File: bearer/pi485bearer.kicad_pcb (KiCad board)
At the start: 2 copper layers, 62 x 30 mm, 21 parts, among them P1 PWR, P2 Rasperry Pi, P3 Latch Disable, P4 TERM, P5 CONN_01X04, P6 CONN_01X04, Q1 2N4401, Q2 2N4401, Q3 2N4401, U1 NE555

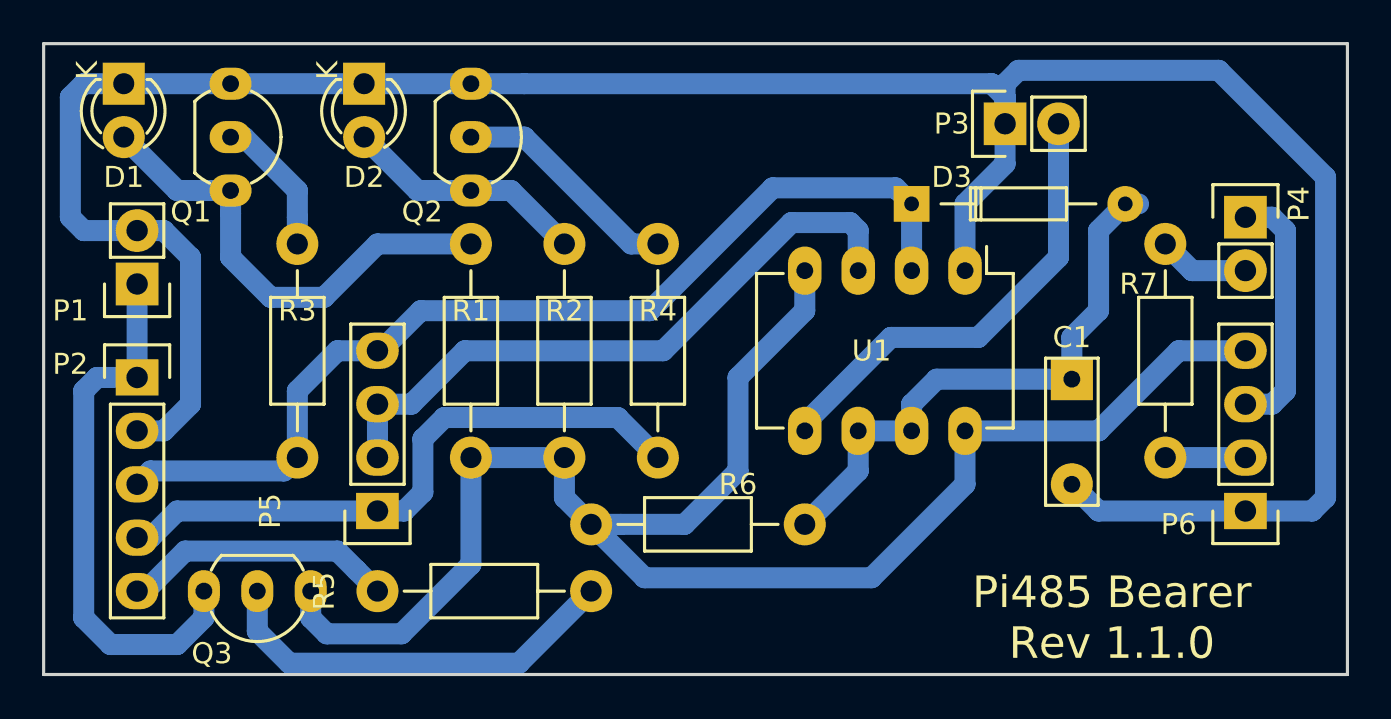
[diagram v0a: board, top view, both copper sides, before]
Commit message: Updated bearer with mount holes
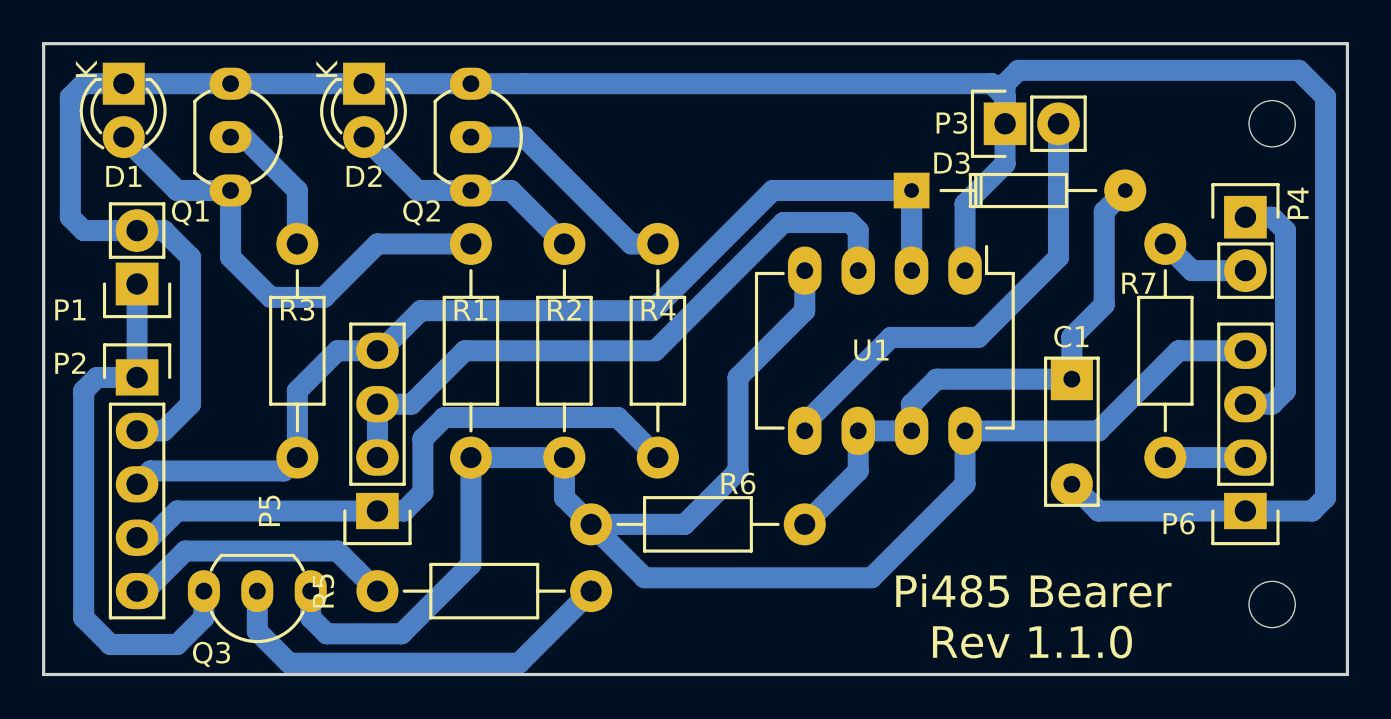
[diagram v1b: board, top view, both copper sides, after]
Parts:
- added MNT01: MountingHole_2.2mm_M2, Mounting_Holes:MountingHole_2.2mm_M2, F.Cu at (95.9, 24.8)
- added MNT02: MountingHole_2.2mm_M2, Mounting_Holes:MountingHole_2.2mm_M2, F.Cu at (95.9, 47.6)
- moved D3 0.63 mm to (78.7, 27.9)
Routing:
- net /(TXDO)_GPIO14: track 48.0 -> 51.7 mm
- net GND: track 123.9 -> 126.1 mm
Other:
- net class Default: trace_width 0.8 -> 1
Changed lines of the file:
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@@
 (kicad_pcb (version 20160815) (host pcbnew "(2016-12-18 revision 3ffa37c)-master")
   (general
-    (links 41)
+    (links 0)
     (no_connects 0)
     (area 37.389999 20.879999 99.540001 51.119002)
@@
     (tracks 142)
     (zones 0)
-    (modules 21)
+    (modules 23)
     (nets 18)
   )
@@
   )
   (setup
-    (last_trace_width 0.8)
+    (last_trace_width 1)
     (trace_clearance 0.2)
     (zone_clearance 0.508)
@@
     (mod_text_width 0.15)
     (pad_size 2 2)
-    (pad_drill 0.8)
+    (pad_drill 0.70104)
     (pad_to_mask_clearance 0.2)
     (aux_axis_origin 37.465 20.955)
@@
   (net_class Default "This is the default net class."
     (clearance 0.2)
-    (trace_width 0.8)
+    (trace_width 1)
     (via_dia 0.8)
     (via_drill 0.4)
@@
     (uvia_drill 0.1)
     (diff_pair_gap 0.2)
-    (diff_pair_width 0.8)
+    (diff_pair_width 1)
     (add_net "/(485PWR)_GPIO18")
     (add_net "/(RXDO)_GPIO15")
@@
     (add_net "Net-(Q3-Pad2)")
     (add_net VCC)
+  )
+  (module Mounting_Holes:MountingHole_2.2mm_M2 (layer F.Cu)
+    (at 95.885 47.625)
+    (descr "Mounting Hole 2.2mm, no annular, M2")
+    (tags "mounting hole 2.2mm no annular m2")
+    (fp_text reference MNT02 (at 0 -3.2) (layer F.SilkS) hide
+      (effects (font (size 1 1) (thickness 0.15)))
+    )
+    (fp_text value MountingHole_2.2mm_M2 (at 0 3.2) (layer F.Fab) hide
+      (effects (font (size 1 1) (thickness 0.15)))
+    )
+    (fp_circle (center 0 0) (end 2.2 0) (layer Cmts.User) (width 0.15))
+    (fp_circle (center 0 0) (end 2.45 0) (layer F.CrtYd) (width 0.05))
+    (pad 1 np_thru_hole circle (at 0 0) (size 2.2 2.2) (drill 2.2) (layers *.Cu *.Mask))
+  )
+  (module Mounting_Holes:MountingHole_2.2mm_M2 (layer F.Cu)
+    (at 95.885 24.765)
+    (descr "Mounting Hole 2.2mm, no annular, M2")
+    (tags "mounting hole 2.2mm no annular m2")
+    (fp_text reference MNT01 (at 0 -3.2) (layer F.SilkS) hide
+      (effects (font (size 1 1) (thickness 0.15)))
+    )
+    (fp_text value MountingHole_2.2mm_M2 (at 0 3.2) (layer F.Fab) hide
+      (effects (font (size 1 1) (thickness 0.15)))
+    )
+    (fp_circle (center 0 0) (end 2.45 0) (layer F.CrtYd) (width 0.05))
+    (fp_circle (center 0 0) (end 2.2 0) (layer Cmts.User) (width 0.15))
+    (pad 1 np_thru_hole circle (at 0 0) (size 2.2 2.2) (drill 2.2) (layers *.Cu *.Mask))
   )
   (module TO_SOT_Packages_THT:TO-92_Inline_Wide (layer F.Cu)
@@
   )
   (module Diodes_THT:Diode_DO-35_SOD27_Horizontal_RM10 (layer F.Cu)
-    (at 78.73948 28.57754)
+    (at 78.73948 27.94254)
     (descr "Diode, DO-35,  SOD27, Horizontal, RM 10mm")
     (tags "Diode, DO-35, SOD27, Horizontal, RM 10mm, 1N4148,")
@@
     (fp_line (start 7.36652 -0.76454) (end 2.79452 -0.76454) (layer F.SilkS) (width 0.15))
     (fp_line (start 2.79452 -0.76454) (end 2.79452 -0.00254) (layer F.SilkS) (width 0.15))
-    (pad 2 thru_hole circle (at 10.16052 -0.00254 180) (size 1.69926 1.69926) (drill 0.70104) (layers *.Cu *.Mask)
+    (pad 2 thru_hole circle (at 10.16052 -0.00254 180) (size 2 2) (drill 0.70104) (layers *.Cu *.Mask)
       (net 1 "Net-(C1-Pad1)"))
     (pad 1 thru_hole rect (at 0.00052 -0.00254 180) (size 1.69926 1.69926) (drill 0.70104) (layers *.Cu *.Mask)
@@
   (gr_line (start 99.465 50.955) (end 37.465 50.955) (layer Edge.Cuts) (width 0.15))
   (gr_line (start 99.465 20.955) (end 37.465 20.955) (layer Edge.Cuts) (width 0.15))
-  (gr_text "Pi485 Bearer\nRev 1.1.0" (at 88.265 48.26) (layer F.SilkS)
+  (gr_text "Pi485 Bearer\nRev 1.1.0" (at 84.455 48.26) (layer F.SilkS)
     (effects (font (size 1.5 1.5) (thickness 0.3)))
   )
+  (segment (start 88.9 27.94) (end 87.900001 28.939999) (width 1) (layer B.Cu) (net 1))
+  (segment (start 87.900001 28.939999) (end 87.900001 33.369999) (width 1) (layer B.Cu) (net 1))
+  (segment (start 87.900001 33.369999) (end 86.36 34.91) (width 1) (layer B.Cu) (net 1))
+  (segment (start 86.36 34.91) (end 86.36 36.91) (width 1) (layer B.Cu) (net 1))
   (segment (start 76.2 39.37) (end 76.2 41.275) (width 1) (layer B.Cu) (net 1))
   (segment (start 76.2 41.275) (end 73.66 43.815) (width 1) (layer B.Cu) (net 1))
-  (segment (start 86.36 36.91) (end 86.36 34.925) (width 1) (layer B.Cu) (net 1))
-  (segment (start 86.36 34.925) (end 87.63 33.655) (width 1) (layer B.Cu) (net 1))
-  (segment (start 87.63 33.655) (end 87.63 29.845) (width 1) (layer B.Cu) (net 1))
-  (segment (start 87.63 29.845) (end 88.9 28.575) (width 1) (layer B.Cu) (net 1))
   (segment (start 79.93 36.91) (end 86.36 36.91) (width 1) (layer B.Cu) (net 1))
-  (segment (start 88.9 28.575) (end 89.535 28.575) (width 1) (layer B.Cu) (net 1))
   (segment (start 79.93 36.91) (end 78.74 38.1) (width 1) (layer B.Cu) (net 1))
   (segment (start 78.74 38.1) (end 78.74 39.37) (width 1) (layer B.Cu) (net 1))
@@
   (segment (start 94.615 43.18) (end 97.79 43.18) (width 1) (layer B.Cu) (net 2))
   (segment (start 97.79 43.18) (end 98.425 42.545) (width 1) (layer B.Cu) (net 2))
-  (segment (start 98.425 42.545) (end 98.425 27.305) (width 1) (layer B.Cu) (net 2))
-  (segment (start 98.425 27.305) (end 93.345 22.225) (width 1) (layer B.Cu) (net 2))
-  (segment (start 93.345 22.225) (end 83.82 22.225) (width 1) (layer B.Cu) (net 2))
+  (segment (start 98.425 42.545) (end 98.425 23.495) (width 1) (layer B.Cu) (net 2))
+  (segment (start 98.425 23.495) (end 97.155 22.225) (width 1) (layer B.Cu) (net 2))
+  (segment (start 97.155 22.225) (end 83.82 22.225) (width 1) (layer B.Cu) (net 2))
   (segment (start 83.82 22.225) (end 83.185 22.86) (width 1) (layer B.Cu) (net 2))
   (segment (start 83.185 22.86) (end 83.185 24.765) (width 1) (layer B.Cu) (net 2))
@@
   (segment (start 53.34 35.56) (end 53.4924 35.56) (width 1) (layer B.Cu) (net 5))
   (segment (start 53.4924 35.56) (end 55.3974 33.655) (width 1) (layer B.Cu) (net 5))
-  (segment (start 55.3974 33.655) (end 66.294 33.655) (width 1) (layer B.Cu) (net 5))
-  (segment (start 66.294 33.655) (end 72.136 27.813) (width 1) (layer B.Cu) (net 5))
-  (segment (start 72.136 27.813) (end 77.978 27.813) (width 1) (layer B.Cu) (net 5))
-  (segment (start 77.978 27.813) (end 78.74 28.575) (width 1) (layer B.Cu) (net 5))
+  (segment (start 55.3974 33.655) (end 66.421 33.655) (width 1) (layer B.Cu) (net 5))
+  (segment (start 66.421 33.655) (end 72.136 27.94) (width 1) (layer B.Cu) (net 5))
+  (segment (start 72.136 27.94) (end 78.105 27.94) (width 1) (layer B.Cu) (net 5))
+  (segment (start 78.105 27.94) (end 78.74 28.575) (width 1) (layer B.Cu) (net 5))
+  (segment (start 78.74 28.575) (end 78.74 31.75) (width 1) (layer B.Cu) (net 5))
+  (segment (start 78.74 31.75) (end 78.74 27.94) (width 1) (layer B.Cu) (net 5))
   (segment (start 41.91 41.91) (end 42.545 41.275) (width 1) (layer B.Cu) (net 5))
   (segment (start 42.545 41.275) (end 48.895 41.275) (width 1) (layer B.Cu) (net 5))
@@
   (segment (start 49.53 37.465) (end 51.435 35.56) (width 1) (layer B.Cu) (net 5))
   (segment (start 51.435 35.56) (end 53.34 35.56) (width 1) (layer B.Cu) (net 5))
-  (segment (start 78.74 28.575) (end 78.74 31.75) (width 1) (layer B.Cu) (net 5))
   (segment (start 45.085 46.99) (end 45.085 48.26) (width 1) (layer B.Cu) (net 6))
   (segment (start 45.085 48.26) (end 43.815 49.53) (width 1) (layer B.Cu) (net 6))
@@
   (segment (start 66.675 40.64) (end 64.77 38.735) (width 1) (layer B.Cu) (net 7))
   (segment (start 64.77 38.735) (end 56.515 38.735) (width 1) (layer B.Cu) (net 7))
+  (segment (start 54.61 43.18) (end 53.34 43.18) (width 1) (layer B.Cu) (net 7))
   (segment (start 56.515 38.735) (end 55.499 39.751) (width 1) (layer B.Cu) (net 7))
   (segment (start 55.499 39.751) (end 55.499 42.291) (width 1) (layer B.Cu) (net 7))
   (segment (start 55.499 42.291) (end 54.61 43.18) (width 1) (layer B.Cu) (net 7))
-  (segment (start 54.61 43.18) (end 53.34 43.18) (width 1) (layer B.Cu) (net 7))
   (segment (start 41.91 44.45) (end 42.545 44.45) (width 1) (layer B.Cu) (net 7))
   (segment (start 42.545 44.45) (end 43.815 43.18) (width 1) (layer B.Cu) (net 7))
@@
   (segment (start 76.2 31.75) (end 76.2 29.845028) (width 1) (layer B.Cu) (net 15))
   (segment (start 76.2 29.845028) (end 75.818972 29.464) (width 1) (layer B.Cu) (net 15))
-  (segment (start 75.818972 29.464) (end 73.025 29.464) (width 1) (layer B.Cu) (net 15))
-  (segment (start 73.025 29.464) (end 66.929 35.56) (width 1) (layer B.Cu) (net 15))
-  (segment (start 66.929 35.56) (end 57.496 35.56) (width 1) (layer B.Cu) (net 15))
+  (segment (start 66.548 35.56) (end 57.496 35.56) (width 1) (layer B.Cu) (net 15))
   (segment (start 57.496 35.56) (end 54.956 38.1) (width 1) (layer B.Cu) (net 15))
   (segment (start 54.956 38.1) (end 53.34 38.1) (width 1) (layer B.Cu) (net 15))
+  (segment (start 75.818972 29.464) (end 72.644 29.464) (width 1) (layer B.Cu) (net 15))
+  (segment (start 72.644 29.464) (end 66.548 35.56) (width 1) (layer B.Cu) (net 15))
   (segment (start 53.34 38.1) (end 53.34 40.64) (width 1) (layer B.Cu) (net 15))
   (segment (start 94.615 40.64) (end 90.805 40.64) (width 1) (layer B.Cu) (net 16))

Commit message: Trace revisions....
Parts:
- added MNT01: MountingHole_2.2mm_M2, Mounting_Holes:MountingHole_2.2mm_M2, F.Cu at (66.5, 23.5)
- moved R6 7.24 mm to (67.9, 48.3)
- moved R5 4.94 mm to (67.9, 44.8)
- moved MNT01 1.42 mm to (96.5, 23.5)
- moved R4 1.27 mm to (67.9, 30.5)
- moved MNT02 0.90 mm to (96.5, 48.3)
- moved R2 0.51 mm to (62.7, 30.5)
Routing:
- net Net-(C1-Pad1): track 27.4 -> 35.9 mm
- net /lctec485/VCIN: track 80.8 -> 72.3 mm, vias 0 -> 2
- net Net-(Q3-Pad2): track 19.8 -> 24.9 mm
- net /(485PWR)_GPIO18: track 13.0 -> 17.6 mm
- net /(TXDO)_GPIO14: track 51.7 -> 54.0 mm
- net /lctec485/DE: track 31.0 -> 33.1 mm
- net /(RXDO)_GPIO15: track 30.4 -> 32.0 mm
- net GND: track 126.1 -> 124.5 mm
- net Net-(Q2-Pad2): track 11.0 -> 12.3 mm
- net Net-(D2-Pad2): track 11.6 -> 12.8 mm
